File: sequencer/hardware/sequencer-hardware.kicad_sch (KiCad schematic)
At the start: 46 parts

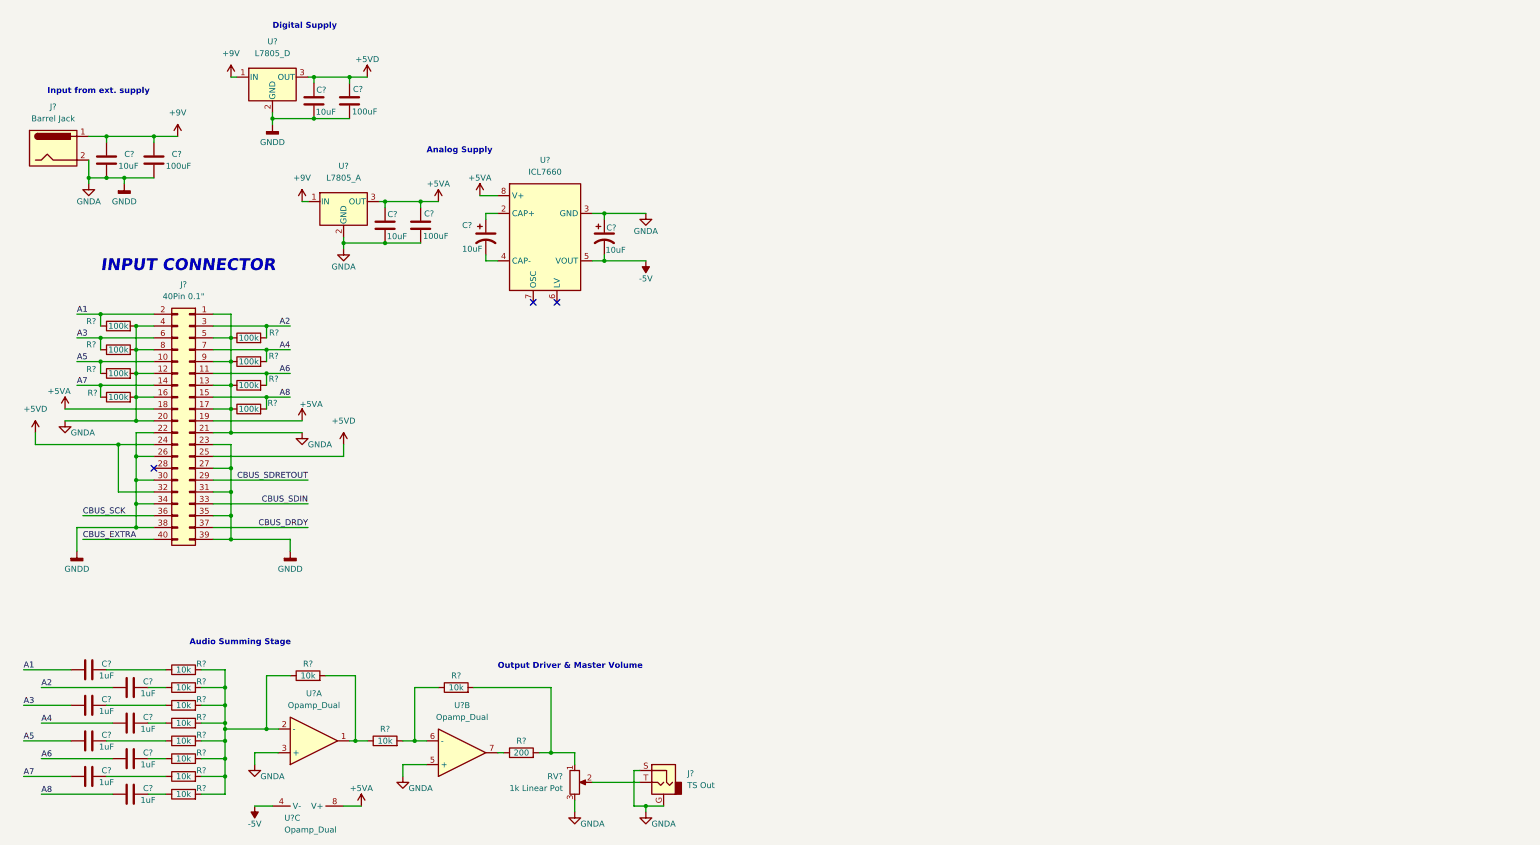
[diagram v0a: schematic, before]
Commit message: transferred digital system to sequencer schematic
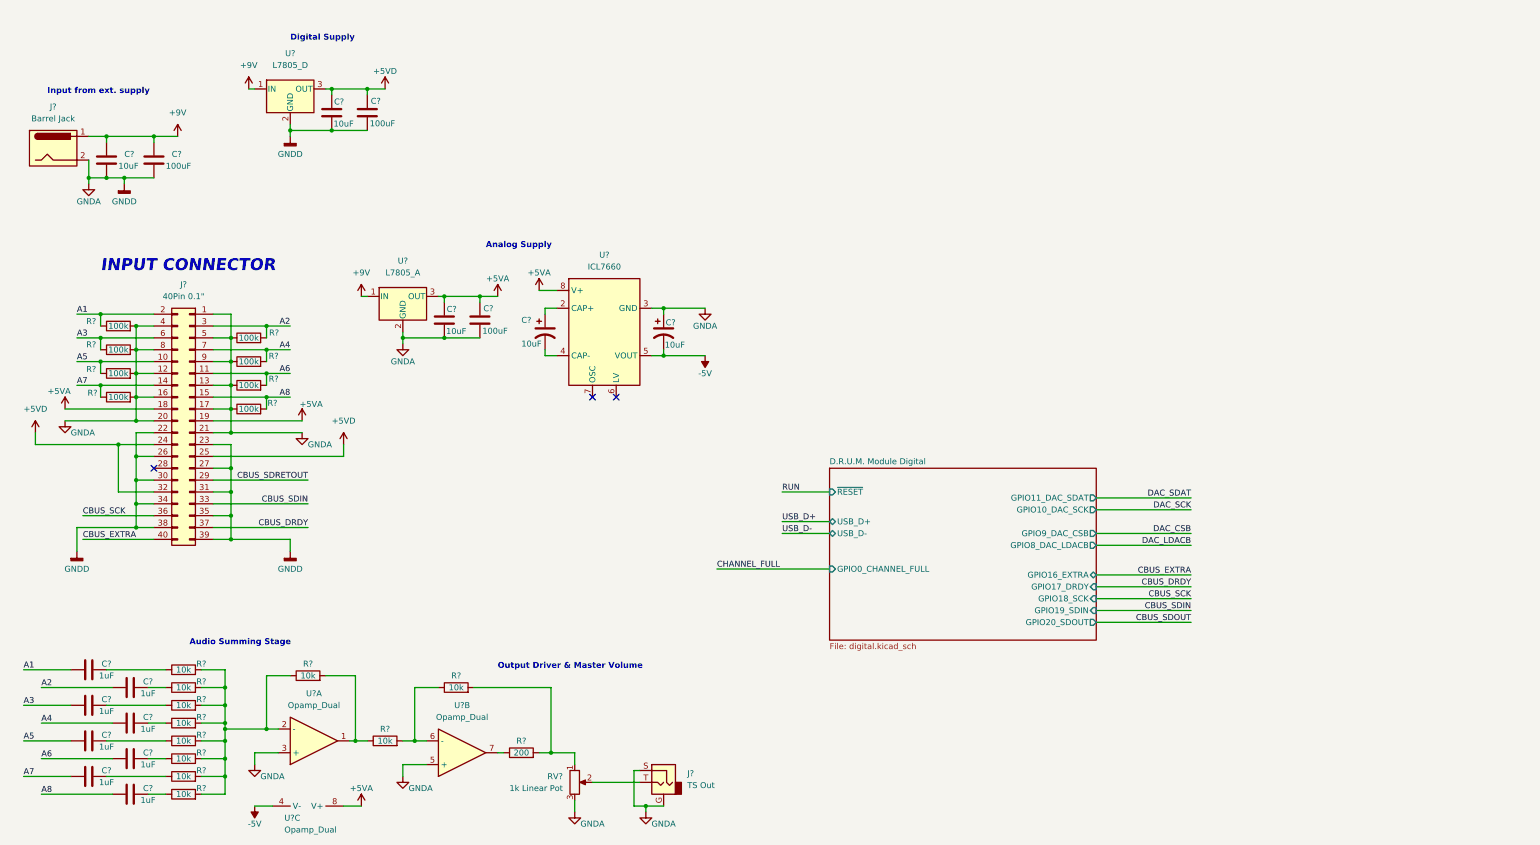
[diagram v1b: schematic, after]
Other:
- added sheet D.R.U.M. Module Digital (digital.kicad_sch)
- moved on the sheet: C?, U?

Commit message: Finish Sequencer Schematic
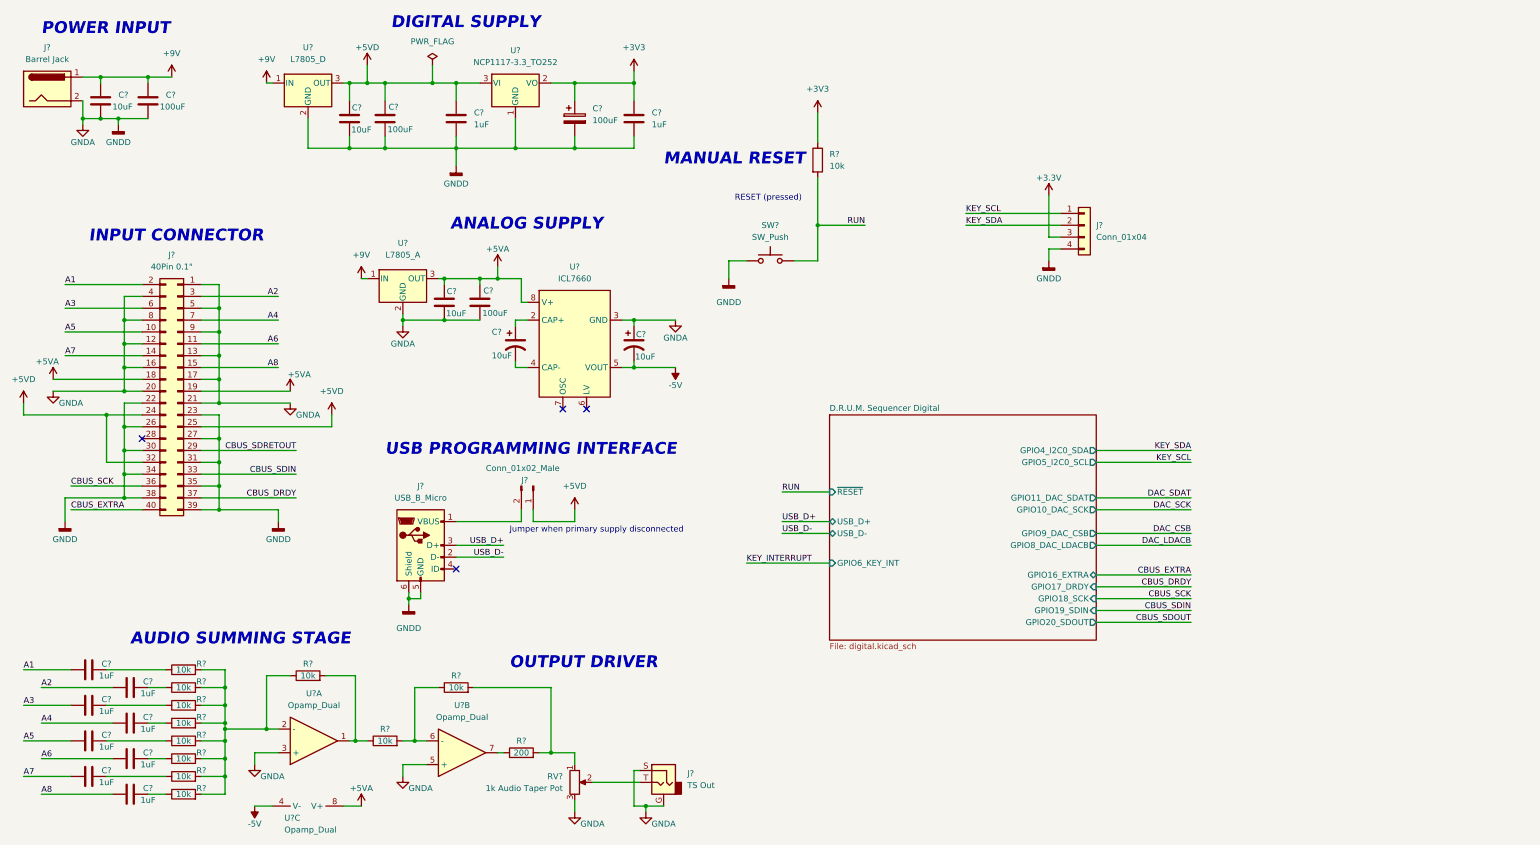
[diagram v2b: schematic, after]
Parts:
- removed R? (x8): 100k, symbol Device:R
- added C?: 100uF, Capacitor_THT:CP_Radial_D8.0mm_P3.50mm, symbol Device:C_Polarized
- added C? (x2): 1uF, Capacitor_SMD:C_0603_1608Metric_Pad1.08x0.95mm_HandSolder, symbol Device:C
- added J?: USB_B_Micro, Connector_USB:USB_Micro-B_Amphenol_10104110_Horizontal, symbol Connector:USB_B_Micro
- added J?: Conn_01x04, symbol Connector_Generic:Conn_01x04
- added J?: Conn_01x02_Male, Connector_PinHeader_2.54mm:PinHeader_1x02_P2.54mm_Vertical, symbol Connector:Conn_01x02_Male
- added R?: 10k, Resistor_SMD:R_0603_1608Metric_Pad0.98x0.95mm_HandSolder, symbol Device:R
- added SW?: SW_Push, custom:TE_ConnMSLPT5252CG1, symbol Switch:SW_Push
- added U?: NCP1117-3.3_TO252, Package_TO_SOT_SMD:TO-252-2, symbol Regulator_Linear:NCP1117-3.3_TO252
- RV?: value 1k Linear Pot -> 1k Audio Taper Pot
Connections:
- net +5VD: now also C?.1, J?.1 (Pin_1), U?.3 (VI)
- net GNDA: now also C?.2, C?.2, C?.2, J?.4 (Pin_4), J?.5 (GND), J?.6 (Shield), SW?.1, U?.1 (GND)
- net RUN: now also R?.2, SW?.2
- net USB_D+: now also J?.3 (D+)
- net USB_D-: now also J?.2 (D-)
- new net: J?.1 (VBUS), J?.2 (Pin_2)
- new net +3V3: C?.1, C?.1, J?.3 (Pin_3), R?.1, U?.2 (VO)
- new net KEY_SCL: J?.1 (Pin_1)
- new net KEY_SDA: J?.2 (Pin_2)
- no-connect marks 3 -> 4
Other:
- sheet D.R.U.M. Module Digital renamed D.R.U.M. Sequencer Digital
- sheet D.R.U.M. Sequencer Digital ports: added GPIO4_I2C0_SDA, GPIO5_I2C0_SCL, GPIO6_KEY_INT; removed GPIO0_CHANNEL_FULL
- note added: "ANALOG SUPPLY"
- note added: "AUDIO SUMMING STAGE"
- note added: "DIGITAL SUPPLY"
- note added: "Jumper when primary supply disconnected"
- note added: "MANUAL RESET"
- note added: "OUTPUT DRIVER"
- note added: "POWER INPUT"
- note added: "RESET (pressed)"
- note added: "USB PROGRAMMING INTERFACE"
- note removed: "Analog Supply"
- note removed: "Audio Summing Stage"
- note removed: "Digital Supply"
- note removed: "Input from ext. supply"
- note removed: "Output Driver & Master Volume"
- moved on the sheet: C?, J?, U?

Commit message: Update sequencer schematic
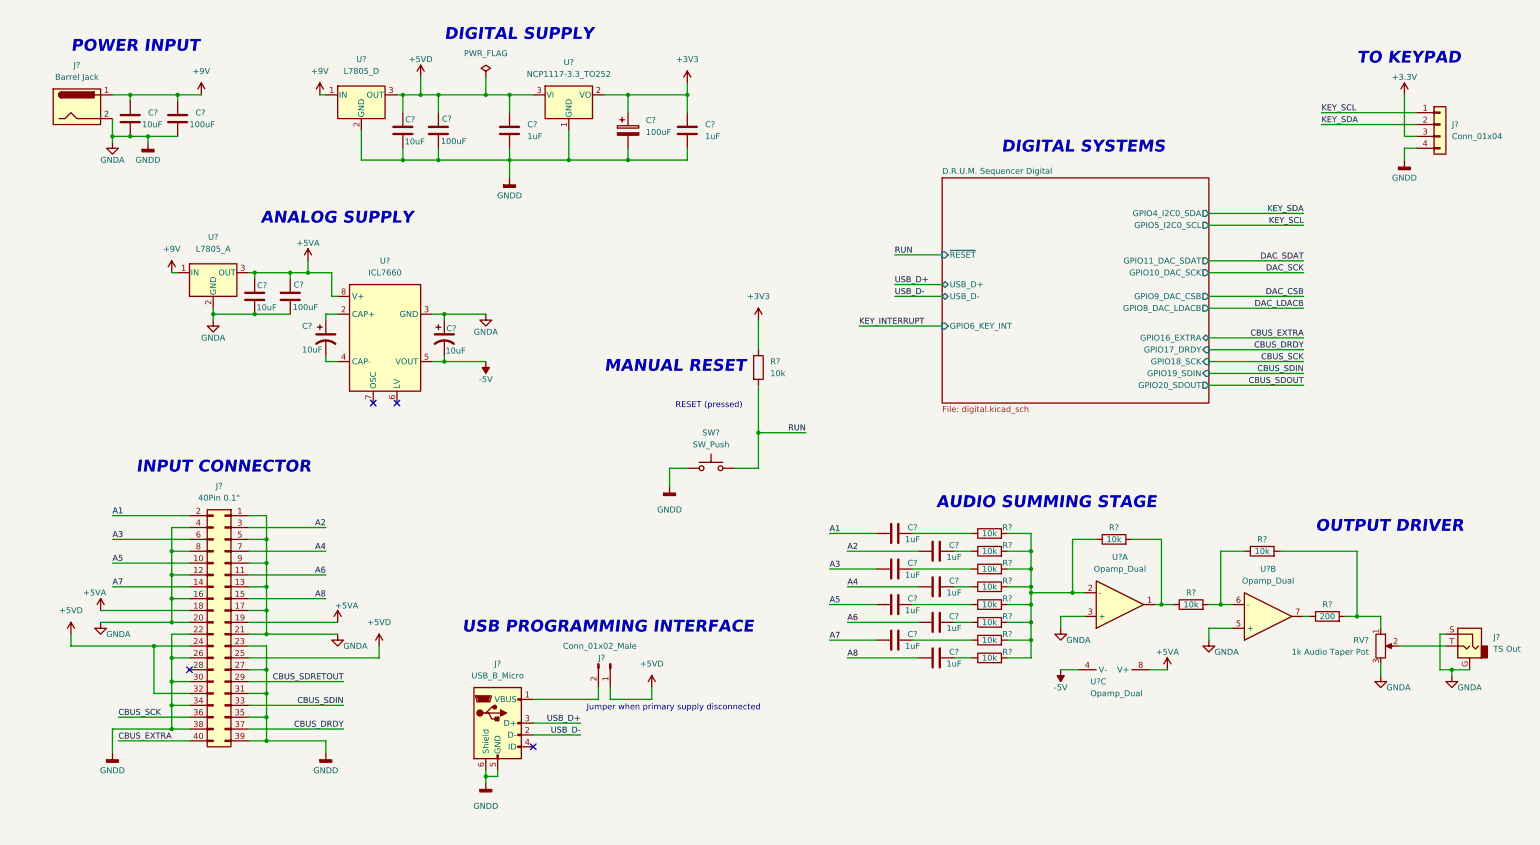
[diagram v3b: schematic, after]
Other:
- note added: "DIGITAL SYSTEMS"
- note added: "TO KEYPAD"
- moved on the sheet: C?, J?, R?, RV?, SW?, U?, U?A, U?B, U?C

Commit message: Implement changes to sequencer recommended by John
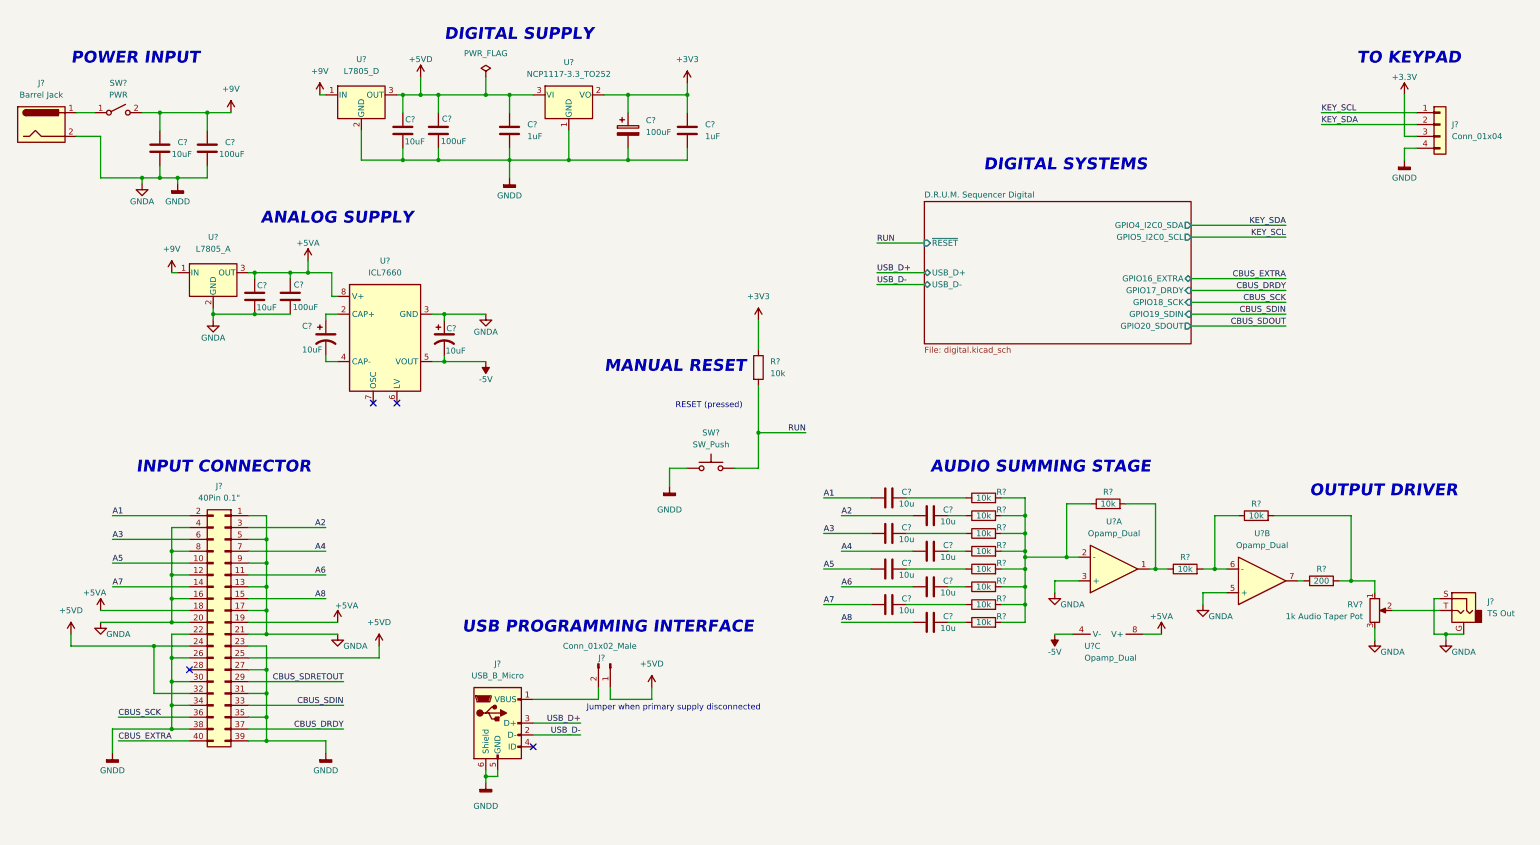
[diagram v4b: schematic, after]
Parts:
- added SW?: PWR, symbol Switch:SW_SPST
- C? (x8): value 1uF -> 10u
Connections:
- net +9V: now also SW?.2 (B); no longer J?.1
- new net: J?.1, SW?.1 (A)
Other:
- sheet D.R.U.M. Sequencer Digital ports: added none; removed GPIO10_DAC_SCK, GPIO11_DAC_SDAT, GPIO6_KEY_INT, GPIO8_DAC_LDACB, GPIO9_DAC_CSB
- moved on the sheet: C?, J?, R?, RV?, U?A, U?B, U?C

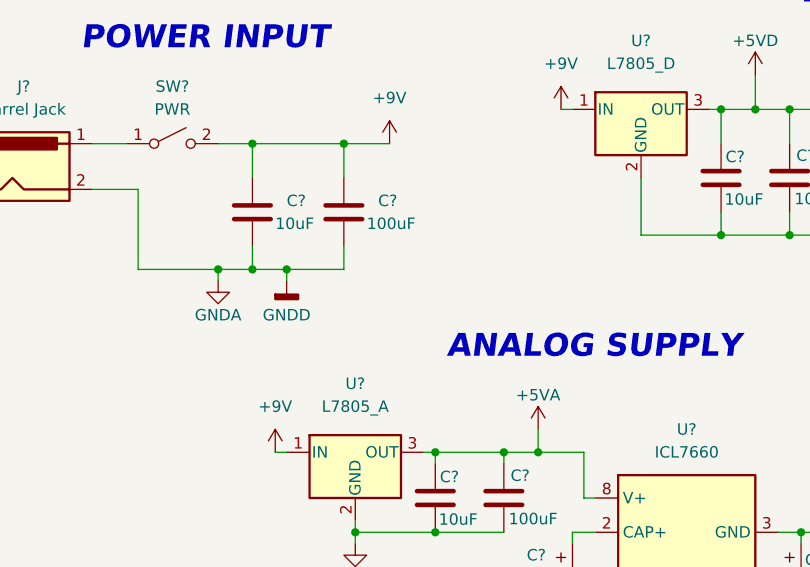
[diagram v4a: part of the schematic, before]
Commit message: Denote start ground point
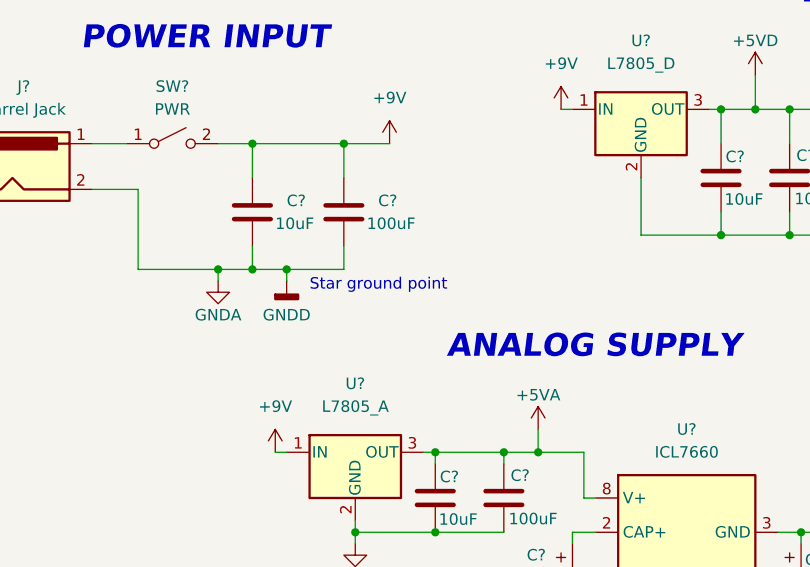
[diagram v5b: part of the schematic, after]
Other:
- note added: "Star ground point"
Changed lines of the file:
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@@
     (effects (font (size 2.54 2.54) (thickness 0.508) bold italic) (justify left bottom))
+  )
+  (text "Star ground point" (at 52.07 54.61 0)
+    (effects (font (size 1.27 1.27)) (justify left bottom))
   )
   (label "A2" (at 81.28 127 180)
